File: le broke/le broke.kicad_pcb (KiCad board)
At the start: 2 copper layers, 99.7 x 75.9 mm, 37 parts, among them U1 ProMicro

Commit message: did a lebroke thing idk
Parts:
- added REF**: MountingHole_2.2mm_M2, MountingHole:MountingHole_2.2mm_M2, F.Cu at (98.1, 56.1)
- added REF**: MountingHole_2.2mm_M2, MountingHole:MountingHole_2.2mm_M2, F.Cu at (190.4, 127.0)
- added REF**: MountingHole_2.2mm_M2, MountingHole:MountingHole_2.2mm_M2, F.Cu at (98.1, 127.0)
- added REF**: MountingHole_2.2mm_M2, MountingHole:MountingHole_2.2mm_M2, F.Cu at (161.9, 56.1)
- added SW1: SW_Push, Button_Switch_THT:SW_PUSH_6mm, F.Cu at (172.8, 53.6)
- moved D16 11.0 mm to (145.4, 128.4), turned to 90 degrees
- moved D17 10.9 mm to (166.9, 128.2), turned to 90 degrees
- moved D10 10.8 mm to (109.7, 94.8), turned to 90 degrees
- moved D18 10.8 mm to (185.9, 128.2), turned to 90 degrees
- moved D8 10.8 mm to (166.9, 90.0), turned to 90 degrees
- moved D7 10.8 mm to (128.7, 90.0), turned to 90 degrees
- moved U1 10.7 mm to (195.5, 68.2)
- moved D9 10.5 mm to (184.7, 94.7), turned to 90 degrees
- moved D6 10.4 mm to (147.8, 84.5), turned to 90 degrees
- moved D2 9.39 mm to (128.8, 63.3)
- moved MX5 9.39 mm to (100.2, 73.1)
- moved MX16 9.39 mm to (135.9, 125.5)
- moved MX4 9.39 mm to (176.4, 68.3)
- moved MX9 9.39 mm to (176.4, 87.4)
- moved D1 9.39 mm to (147.8, 58.5)
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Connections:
- D1 pad 2: Net-(D1-A) -> ROW0
- D10 pad 1: Net-(D10-K) -> ROW0
- D11 pad 2: Net-(D11-A) -> ROW1
- D12 pad 2: Net-(D11-A) -> ROW1
- D13 pad 2: Net-(D11-A) -> ROW1
- D14 pad 2: Net-(D11-A) -> ROW1
- D15 pad 2: Net-(D11-A) -> ROW1
- D16 pad 1: Net-(D16-K) -> ROW1
- D17 pad 1: Net-(D17-K) -> ROW1
- D17 pad 2: Net-(D16-A) -> Net-(D17-A)
- D18 pad 1: Net-(D18-K) -> ROW1
- D18 pad 2: Net-(D16-A) -> Net-(D18-A)
- D2 pad 2: Net-(D1-A) -> ROW0
- D3 pad 2: Net-(D1-A) -> ROW0
- D4 pad 2: Net-(D1-A) -> ROW0
- D5 pad 2: Net-(D1-A) -> ROW0
- D6 pad 1: Net-(D6-K) -> ROW0
- D6 pad 2: Net-(D10-A) -> Net-(D6-A)
- D7 pad 1: Net-(D7-K) -> ROW0
- D7 pad 2: Net-(D10-A) -> Net-(D7-A)
- D8 pad 1: Net-(D8-K) -> ROW0
- D8 pad 2: Net-(D10-A) -> Net-(D8-A)
- D9 pad 1: Net-(D9-K) -> ROW0
- D9 pad 2: Net-(D10-A) -> Net-(D9-A)
- MX1 pad 1: Net-(MX1-Pad1) -> COL2
- MX10 pad 1: Net-(MX10-Pad1) -> COL0
- MX10 pad 2: Net-(D10-K) -> Net-(D10-A)
- MX11 pad 1: Net-(MX1-Pad1) -> COL2
- MX12 pad 1: Net-(MX12-Pad1) -> COL1
- MX13 pad 1: Net-(MX13-Pad1) -> COL3
- MX14 pad 1: Net-(MX14-Pad1) -> COL4
- MX15 pad 1: Net-(MX10-Pad1) -> COL0
- MX16 pad 1: Net-(MX1-Pad1) -> COL2
- MX16 pad 2: Net-(D16-K) -> Net-(D16-A)
- MX17 pad 1: Net-(MX13-Pad1) -> COL3
- MX17 pad 2: Net-(D17-K) -> Net-(D17-A)
- MX18 pad 1: Net-(MX14-Pad1) -> COL4
- MX18 pad 2: Net-(D18-K) -> Net-(D18-A)
- MX2 pad 1: Net-(MX12-Pad1) -> COL1
- MX3 pad 1: Net-(MX13-Pad1) -> COL3
- MX4 pad 1: Net-(MX14-Pad1) -> COL4
- MX5 pad 1: Net-(MX10-Pad1) -> COL0
- MX6 pad 1: Net-(MX1-Pad1) -> COL2
- MX6 pad 2: Net-(D6-K) -> Net-(D6-A)
- MX7 pad 1: Net-(MX12-Pad1) -> COL1
- MX7 pad 2: Net-(D7-K) -> Net-(D7-A)
- MX8 pad 1: Net-(MX13-Pad1) -> COL3
- MX8 pad 2: Net-(D8-K) -> Net-(D8-A)
- MX9 pad 1: Net-(MX14-Pad1) -> COL4
- MX9 pad 2: Net-(D9-K) -> Net-(D9-A)
- U1 pad 14: unconnected-(U1-GND-Pad14) -> Net-(SW1-Pad1)
- U1 pad 15: unconnected-(U1-RST-Pad15) -> Net-(U1-RST)
- U1 pad 17: unconnected-(U1-F4-Pad17) -> COL4
- U1 pad 18: unconnected-(U1-F5-Pad18) -> COL3
- U1 pad 19: unconnected-(U1-F6-Pad19) -> COL2
- U1 pad 20: unconnected-(U1-F7-Pad20) -> COL1
- U1 pad 21: unconnected-(U1-B1-Pad21) -> COL0
- U1 pad 22: unconnected-(U1-B3-Pad22) -> ROW0
- U1 pad 23: unconnected-(U1-B2-Pad23) -> ROW1
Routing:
- net ROW0: track 0.00 -> 202.0 mm
- net ROW1: track 0.00 -> 195.2 mm
- net COL0: track 0.00 -> 149.9 mm
- net COL2: track 0.00 -> 142.9 mm
- net COL1: track 0.00 -> 131.0 mm
- net COL3: track 0.00 -> 117.2 mm
- net COL4: track 0.00 -> 91.8 mm
- net Net-(MX1-Pad1): track 91.1 -> 0.00 mm
- net Net-(MX13-Pad1): track 85.3 -> 0.00 mm
- net Net-(MX14-Pad1): track 85.3 -> 0.00 mm
- net Net-(D1-A): track 82.4 -> 0.00 mm
- net Net-(D11-A): track 81.1 -> 0.00 mm
- net Net-(D10-A): track 82.3 -> 13.7 mm
- net Net-(MX10-Pad1): track 59.4 -> 0.00 mm
- net Net-(MX12-Pad1): track 59.4 -> 0.00 mm
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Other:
- board size 99.7 x 75.9 mm -> 100 x 81 mm
- board text added: "reset"
- board text added: "wake"

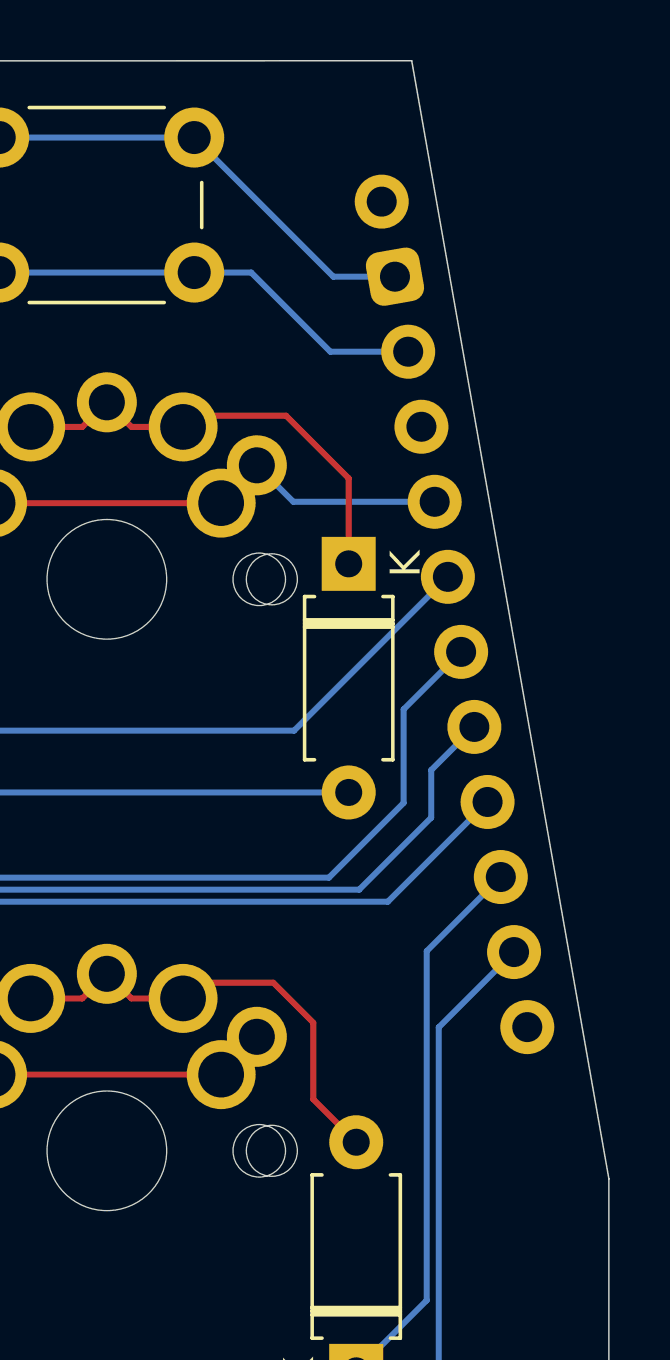
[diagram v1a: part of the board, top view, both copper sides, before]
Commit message: added case DXFs fixed pcb
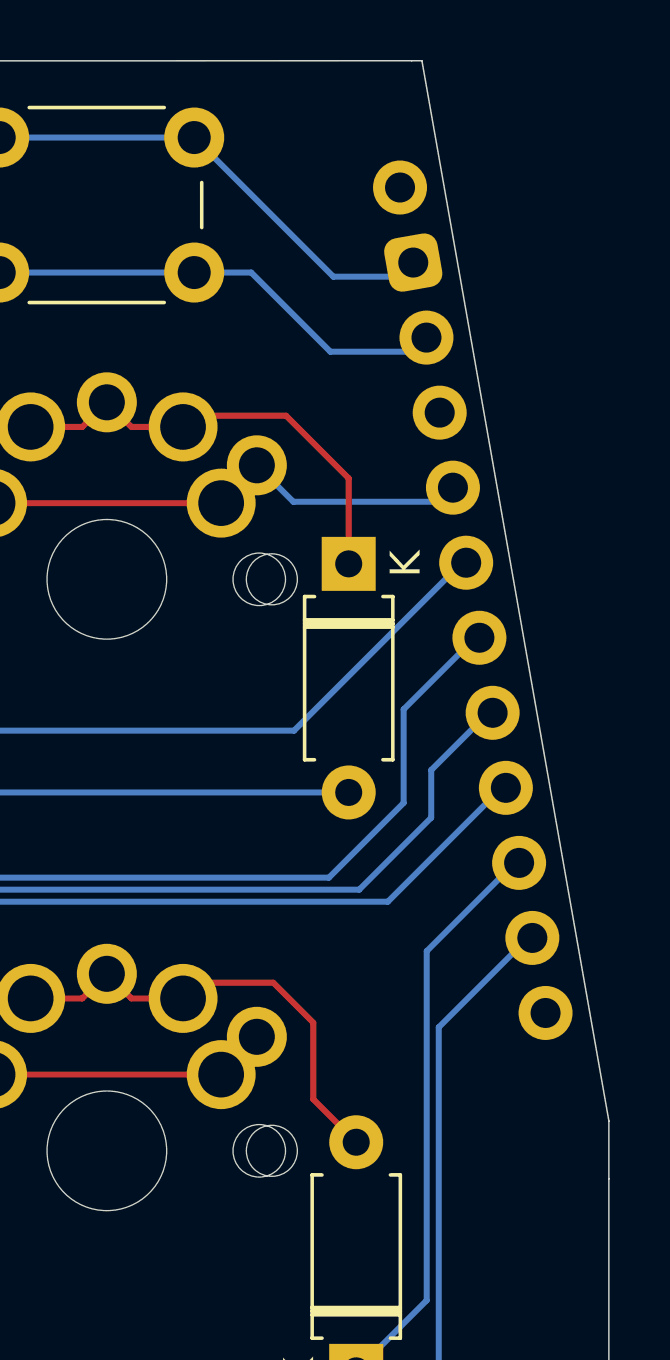
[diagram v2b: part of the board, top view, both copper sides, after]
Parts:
- moved U1 0.77 mm to (196.1, 67.7)
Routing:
- net COL4: track 91.8 -> 92.7 mm
- net Net-(SW1-Pad1): track 15.1 -> 16.0 mm
- net Net-(U1-RST): track 14.7 -> 15.7 mm
- net ROW1: track 195.2 -> 196.0 mm
- net COL3: track 117.2 -> 118.0 mm
- net COL0: track 149.9 -> 150.7 mm
- net ROW0: track 202.0 -> 202.8 mm
- net COL2: track 142.9 -> 143.7 mm
- net COL1: track 131.0 -> 131.8 mm
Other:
- outline, holes or cut-outs redrawn

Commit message: a
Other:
- outline, holes or cut-outs redrawn
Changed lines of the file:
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@@
-	)
-	(gr_line
-		(start 188.1432 131.99679)
-		(end 98.14846 131.996791)
-		(stroke
-			(width 0.05)
-			(type default)
-		)
-		(layer "Edge.Cuts")
 	)
 	(gr_line
@@
 	)
 	(gr_line
-		(start 93.112701 56.050346)
-		(end 93.148458 126.99679)
+		(start 93.172701 56.050346)
+		(end 93.208458 126.99679)
 		(stroke
 			(width 0.05)
@@
 	)
 	(gr_line
+		(start 98.208458 131.996791)
+		(end 188.1432 131.99679)
+		(stroke
+			(width 0.05)
+			(type default)
+		)
+		(layer "Edge.Cuts")
+	)
+	(gr_line
 		(start 186.91049 51.026352)
 		(end 193.143191 86.369326)
@@
 	)
 	(gr_arc
-		(start 93.112701 56.050346)
-		(mid 94.577167 52.514812)
-		(end 98.112701 51.050346)
+		(start 93.172701 56.050346)
+		(mid 94.637169 52.514815)
+		(end 98.172701 51.050346)
+		(stroke
+			(width 0.05)
+			(type default)
+		)
+		(layer "Edge.Cuts")
+	)
+	(gr_line
+		(start 186.57049 51.026444)
+		(end 98.172701 51.050363)
 		(stroke
 			(width 0.05)
@@
 	)
 	(gr_arc
-		(start 98.148458 131.996791)
-		(mid 94.612924 130.532325)
-		(end 93.148458 126.996791)
+		(start 98.208458 131.996791)
+		(mid 94.672954 130.53231)
+		(end 93.208458 126.996791)
 		(stroke
 			(width 0.05)
-			(type default)
-		)
-		(layer "Edge.Cuts")
-	)
-	(gr_line
-		(start 98.112701 51.050346)
-		(end 186.57049 51.026444)
-		(stroke
-			(width 0.05)

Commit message: a
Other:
- board text added: "sleep"
- board text removed: "wake"
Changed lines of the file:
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@@
 			(psa4output no)
 			(plot_black_and_white yes)
+			(plotinvisibletext no)
 			(sketchpadsonfab no)
 			(plotpadnumbers no)
@@
 	)
 	(gr_text "reset"
-		(at 166.20049 56.586444 0)
+		(at 165.89049 56.546444 0)
 		(layer "F.SilkS")
 		(effects
@@
 		)
 	)
-	(gr_text "wake"
-		(at 169.97049 56.606444 0)
+	(gr_text "sleep"
+		(at 169.77049 56.526444 0)
 		(layer "B.SilkS")
 		(effects

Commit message: epic style
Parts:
- D1, D10, D11, D12, D13, D14, D15, D16, D17, D18, D2, D3, D4, D5, D6, D7, D8, D9: footprint Diode_THT:D_A-405_P7.62mm_Horizontal -> isaacscollection:D_A-405_P7.62mm_Horizontal
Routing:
- net ROW1: track 196.0 -> 198.3 mm
- added copper zone on B.Cu, net (none)
- added copper zone on F.Cu, net (none)
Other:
- board text added: "le broke"
